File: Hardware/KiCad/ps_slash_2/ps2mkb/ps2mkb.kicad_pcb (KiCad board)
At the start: 4 copper layers, 112 x 78.8 mm, 27 parts, among them J1 Conn_01x16_Socket, SW1 SW_DIP_x08, U1 74HC126, U11 74HC32, U2 74HC573, U3 74HC688, U4 74HC573, U5 74HC03, U6 74HC04, U9 74HC74

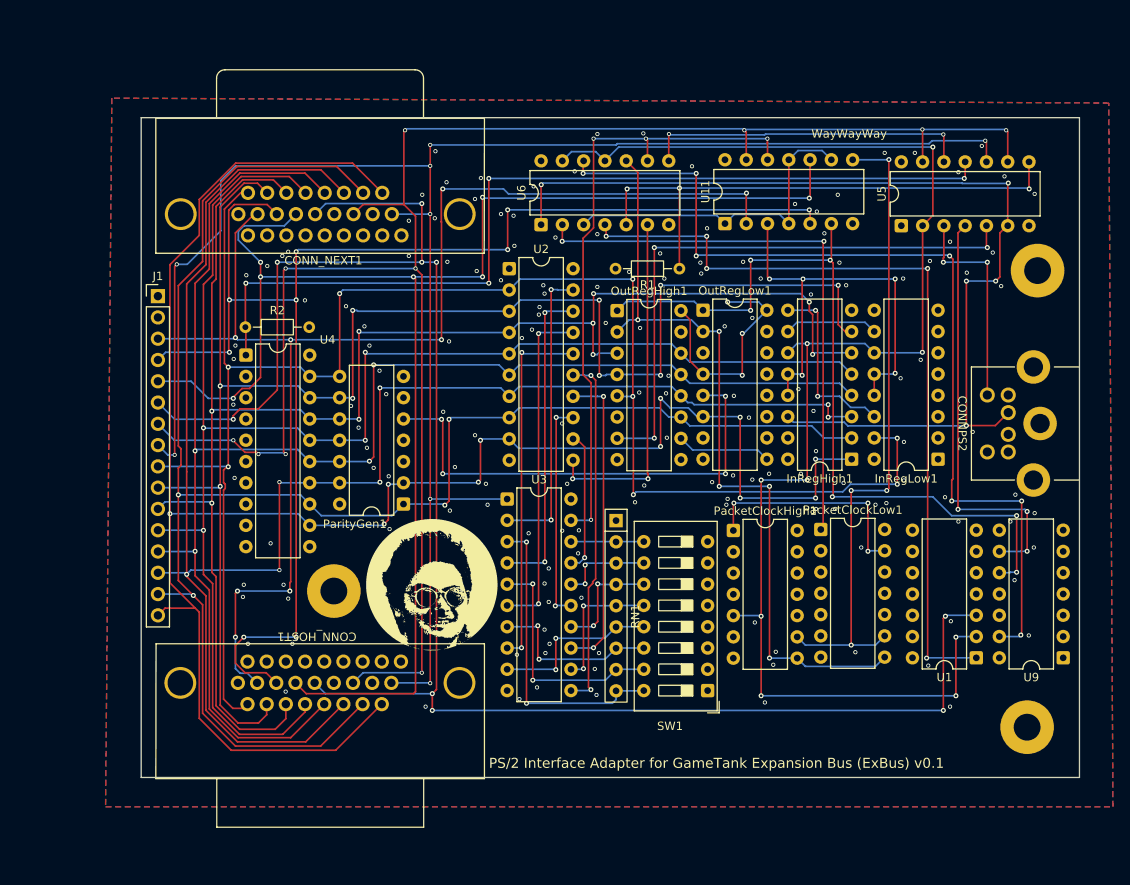
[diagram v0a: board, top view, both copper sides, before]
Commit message: backplane and updated mouse keyboard adapter
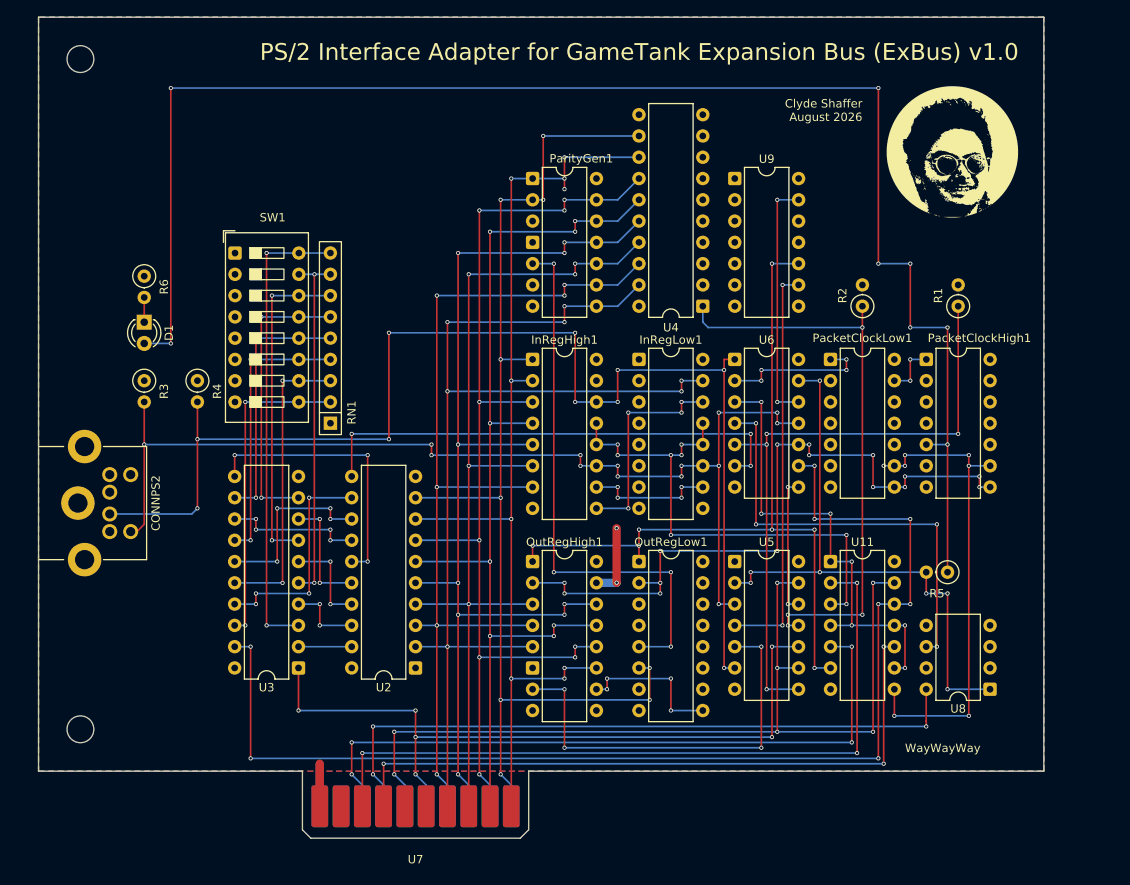
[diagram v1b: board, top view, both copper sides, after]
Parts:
- removed CONN_HOST1: Conn_01x26_Shielded, Library:DB26MALE
- removed CONN_NEXT1: Conn_01x26_Shielded, Library:HDL26-SL-B
- removed H1, H2, H3: MountingHole_Pad, MountingHole:MountingHole_3.2mm_M3_Pad
- removed J1: Conn_01x16_Socket, Connector_PinHeader_2.54mm:PinHeader_1x16_P2.54mm_Vertical
- removed U1: 74HC126, Package_DIP:DIP-14_W7.62mm
- added D1: LED, LED_THT:LED_D3.0mm, F.Cu at (57.6, 88.4)
- added R3: R_US, Resistor_THT:R_Axial_DIN0207_L6.3mm_D2.5mm_P2.54mm_Vertical, F.Cu at (57.6, 95.4)
- added R4: R_US, Resistor_THT:R_Axial_DIN0207_L6.3mm_D2.5mm_P2.54mm_Vertical, F.Cu at (64.0, 95.4)
- added R5: R_US, Resistor_THT:R_Axial_DIN0207_L6.3mm_D2.5mm_P2.54mm_Vertical, F.Cu at (153.5, 118.2)
- added R6: R_US, Resistor_THT:R_Axial_DIN0207_L6.3mm_D2.5mm_P2.54mm_Vertical, F.Cu at (57.6, 82.9)
- added REF**: MountingHole_3.2mm_M3, MountingHole:MountingHole_3.2mm_M3, F.Cu at (50.0, 57.0)
- added REF**: MountingHole_3.2mm_M3, MountingHole:MountingHole_3.2mm_M3, F.Cu at (50.0, 137.0)
- added U7: ~, Library:ExBus_Edge, F.Cu at (90.0, 150.0)
- added U8: TS12A4515P, Package_DIP:DIP-8_W7.62mm, F.Cu at (158.6, 132.2)
- R1, R2: footprint Resistor_THT:R_Axial_DIN0204_L3.6mm_D1.6mm_P7.62mm_Horizontal -> Resistor_THT:R_Axial_DIN0207_L6.3mm_D2.5mm_P2.54mm_Vertical
- moved CONNPS2 124.6 mm to (45.0, 110.0), turned to 90 degrees
- moved G*** 80.8 mm to (154.1, 68.1)
- moved SW1 76.9 mm to (68.5, 80.2), turned to 0 degrees
- moved R2 73.7 mm to (143.3, 86.5), turned to 90 degrees
- moved U9 69.4 mm to (128.1, 71.3), turned to 0 degrees
- moved U4 54.9 mm to (124.3, 86.5), turned to 180 degrees
- moved U2 49.0 mm to (90.0, 129.7), turned to 180 degrees
- moved U5 44.8 mm to (128.1, 117.0), turned to 0 degrees
- moved U11 42.3 mm to (139.5, 117.0), turned to 0 degrees
- moved ParityGen1 41.8 mm to (104.0, 71.3), turned to 0 degrees
- moved InRegHigh1 39.9 mm to (104.0, 92.8), turned to 0 degrees
- moved InRegLow1 37.6 mm to (116.7, 92.8), turned to 0 degrees
- moved RN1 36.0 mm to (79.8, 100.5), turned to 90 degrees
- moved R1 33.6 mm to (154.8, 86.5), turned to 90 degrees
- moved U3 32.0 mm to (76.0, 129.7), turned to 180 degrees
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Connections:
- CONNPS2 pad 5: Net-(CONNPS2-Pad5) -> Net-(InRegHigh1-SRCLK)
- InRegHigh1 pad 11: /Root/PA6 -> Net-(InRegHigh1-SRCLK)
- InRegLow1 pad 11: /Root/PA6 -> Net-(InRegHigh1-SRCLK)
- PacketClockHigh1 pad 5: /Root/PA6 -> Net-(D1-A)
- U5 pad 3: Net-(CONNPS2-Pad5) -> Net-(InRegHigh1-SRCLK)
- U6 pad 11: /Root/PA6 -> Net-(InRegHigh1-SRCLK)
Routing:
- net Net-(CONN_HOST1-Pin_14): track 215.7 -> 0.00 mm, vias 9 -> 0
- net Net-(D1-A): track 0.00 -> 186.7 mm, vias 0 -> 8
- net /Root/CB2: track 215.7 -> 87.5 mm, vias 8 -> 6
- net Net-(InRegHigh1-SRCLK): track 0.00 -> 126.4 mm, vias 0 -> 14
- net /Root/CA2: track 219.0 -> 109.8 mm, vias 10 -> 7
- net Net-(U7-PA5): track 184.7 -> 80.0 mm, vias 7 -> 3
- net /Root/PA6: track 171.4 -> 71.1 mm, vias 9 -> 7
- net /Root/PB7: track 233.4 -> 133.9 mm, vias 11 -> 9
- net Net-(U7-PA4): track 169.8 -> 81.8 mm, vias 9 -> 4
- net /Root/PB6: track 207.1 -> 119.4 mm, vias 4 -> 9
- net /Root/PB5: track 209.6 -> 122.2 mm, vias 7 -> 9
- net /Root/PB2: track 193.4 -> 107.7 mm, vias 9 -> 5
- net Net-(U9B-~{R}): track 111.7 -> 29.2 mm, vias 7 -> 2
- net /Root/PB1: track 194.1 -> 113.3 mm, vias 9 -> 6
- net Net-(U7-PA6): track 0.00 -> 80.5 mm, vias 0 -> 3
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- added copper zone on B.Cu, net GND
- removed copper zone on In1.Cu, net GND
- removed copper zone on In2.Cu, net GND
- removed copper zone on B.Cu, net VCC
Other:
- board size 112 x 78.8 mm -> 120 x 90 mm
- copper layers 4 -> 2
- board text added: "Clyde Shaffer August 2026"
- board text added: "PS/2 Interface Adapter for GameTank Expansion Bus (ExBus) v1.0"
- board text removed: "PS/2 Interface Adapter for GameTank Expansion Bus (ExBus) v0.1"
